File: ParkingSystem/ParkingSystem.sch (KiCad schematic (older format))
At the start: 73 parts, among them J1 PJ-002A, J2 0430450400, J3 Conn_ARM_JTAG_SWD_10, J4 Conn_01x04_Female, J5 0430450200, SW1 SW_Push, U1 R-78E5.0-1.0, U2 R-783.3-0.5, U3 STM32F103C4Tx, U5 74LS47, U6 74LS47, Y1 Crystal

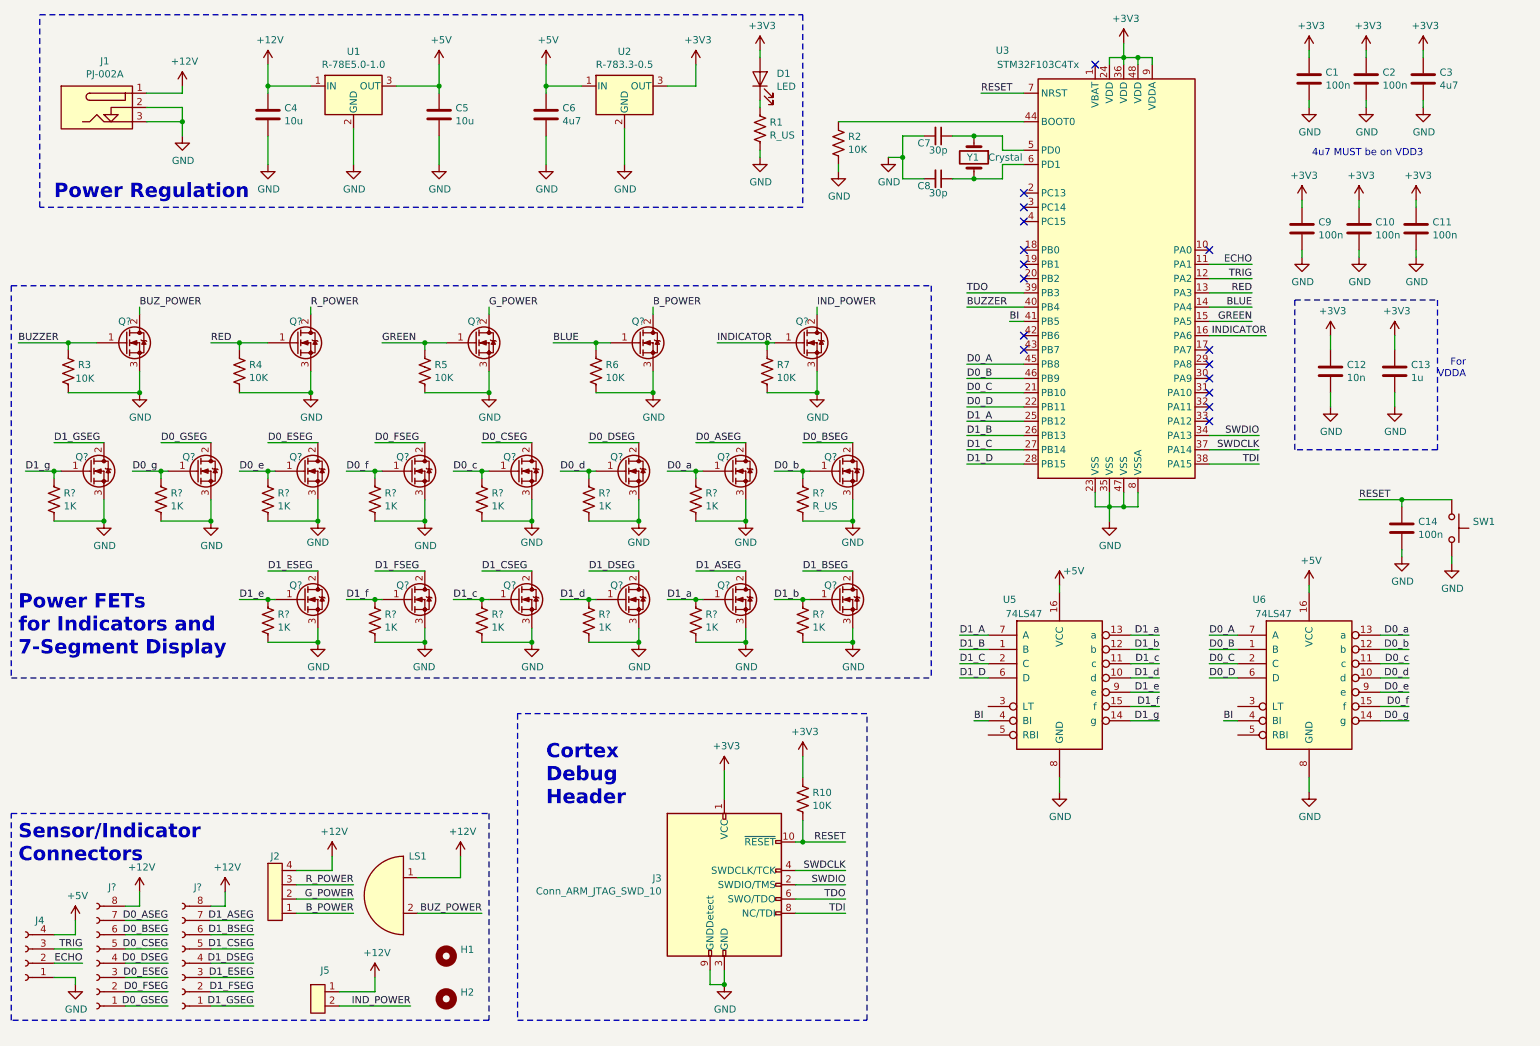
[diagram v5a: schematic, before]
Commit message: Create sn74L47 footprint and begin pcb layout
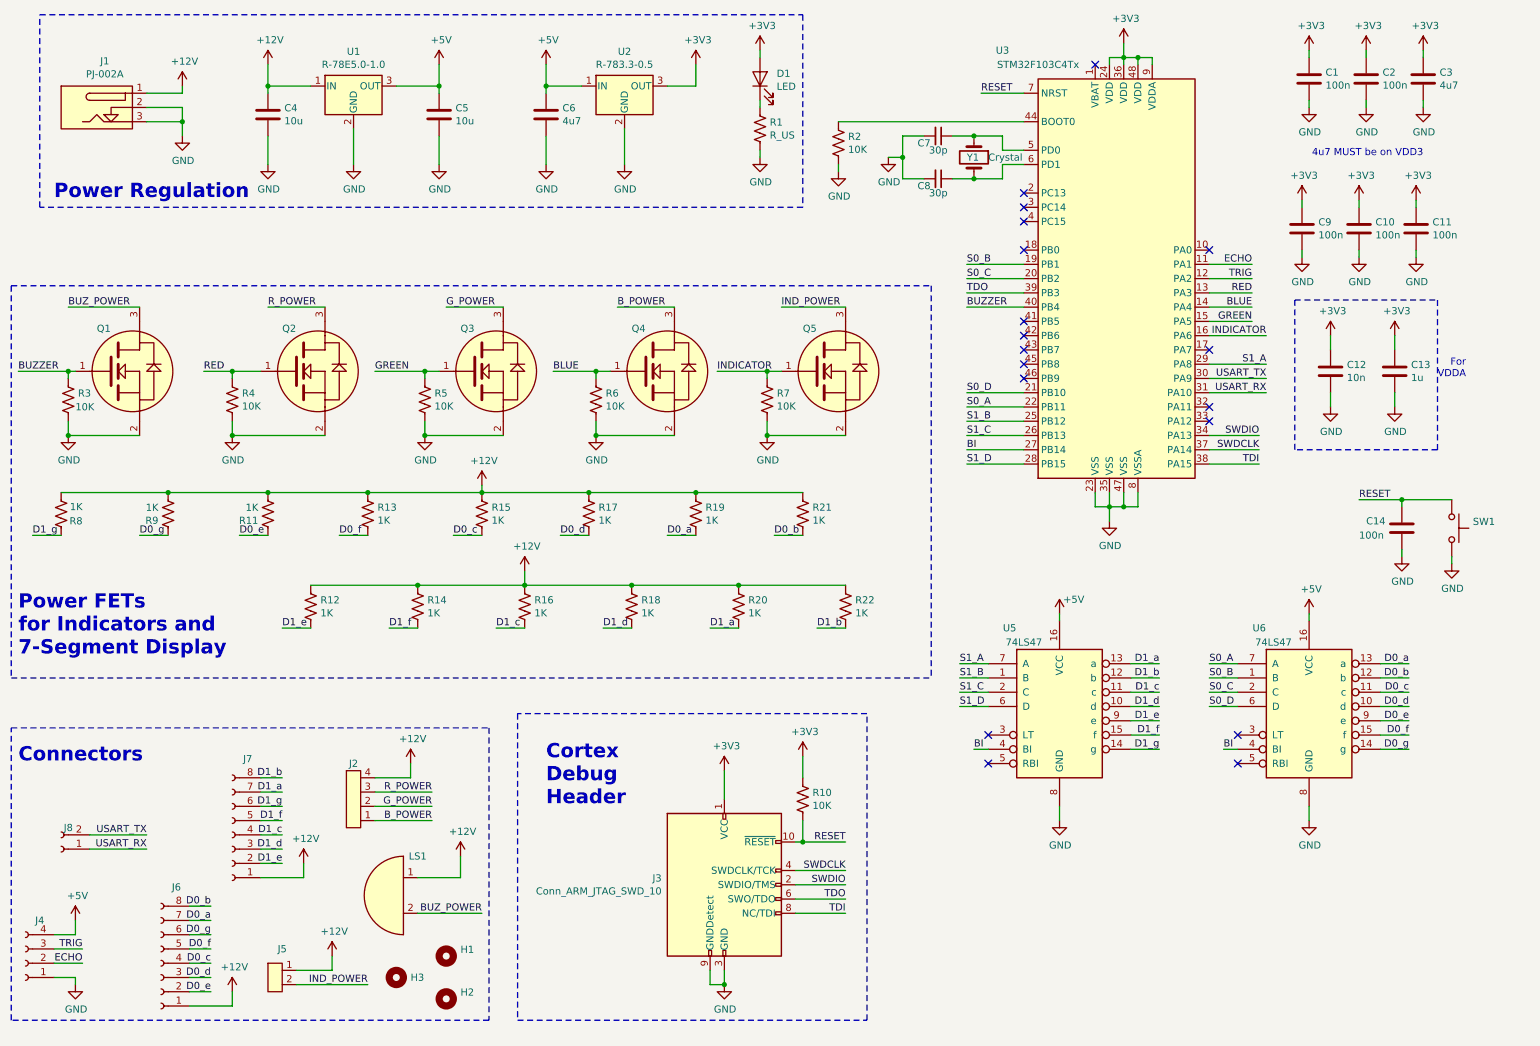
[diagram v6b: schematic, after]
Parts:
- removed Q? (x17): Q_NMOS_GDS, symbol Device:Q_NMOS_GDS
- removed Q? (x2): 1K, symbol Device:Q_NMOS_GDS
- added H3: MountingHole, MountingHole:MountingHole_4.3mm_M4_DIN965_Pad, symbol Mechanical:MountingHole
- added J8: Conn_01x02_Female, Connector_PinHeader_2.54mm:PinHeader_1x02_P2.54mm_Vertical, symbol Connector:Conn_01x02_Female
- added Q1, Q2, Q3, Q4, Q5: SSM3K333R,LF, MOSFETS:SSM3K33R,LF, symbol MOSFETS:SSM3K333R,LF
- J6, J7: renamed from J?; footprint (none) -> Connector_Molex:Molex_Micro-Fit_3.0_43045-0800_2x04_P3.00mm_Horizontal
- R11, R12, R13, R14, R15, R16, R17, R18, R19, R20, R22, R8, R9: renamed from R?; footprint (none) -> Resistor_SMD:R_0603_1608Metric_Pad1.05x0.95mm_HandSolder
- R21: renamed from R?; value R_US -> 1K; footprint (none) -> Resistor_SMD:R_0603_1608Metric_Pad1.05x0.95mm_HandSolder
- U5, U6: footprint (none) -> Drivers:SN74LS47N
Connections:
- net D0_ASEG is gone; now on net D0_a: J6.7 (Pin_7)
- net D0_BSEG is gone; now on net D0_g: J6.6 (Pin_6)
- net D0_CSEG is gone; now on net D0_f: J6.5 (Pin_5)
- net D0_DSEG is gone; now on net D0_c: J6.4 (Pin_4)
- net D0_ESEG is gone; now on net D0_d: J6.3 (Pin_3)
- net D0_FSEG is gone; now on net D0_e: J6.2 (Pin_2)
- net D0_GSEG is gone; now on net +12V: J6.1 (Pin_1)
- net D1_ASEG is gone; now on net D1_a: J7.7 (Pin_7)
- net D1_BSEG is gone; now on net D1_g: J7.6 (Pin_6)
- net D1_CSEG is gone; now on net D1_f: J7.5 (Pin_5)
- net D1_DSEG is gone; now on net D1_c: J7.4 (Pin_4)
- net D1_ESEG is gone; now on net D1_d: J7.3 (Pin_3)
- net D1_FSEG is gone; now on net D1_e: J7.2 (Pin_2)
- net D1_GSEG is gone; now on net +12V: J7.1 (Pin_1)
- net +12V: now also R11.2, R12.1, R13.1, R14.1, R15.1, R16.1, R17.1, R18.1, R19.1, R20.1, R21.1, R22.1, R8.2, R9.2; no longer J6.8 (Pin_8), J7.8 (Pin_8)
- net BI: now also U3.27 (PB14); no longer U3.41 (PB5)
- net BLUE: now also Q4.1
- net BUZZER: now also Q1.1
- net BUZ_POWER: now also Q1.3
- net B_POWER: now also Q4.3
- net D0_a: now also R19.2; no longer R19.1
- net D0_b: now also J6.8 (Pin_8), R21.2; no longer R21.1
- net D0_c: now also R15.2; no longer R15.1
- net D0_d: now also R17.2; no longer R17.1
- net D0_f: now also R13.2; no longer R13.1
- net D1_a: now also R20.2; no longer R20.1
- net D1_b: now also J7.8 (Pin_8), R22.2; no longer R22.1
- net D1_c: now also R16.2; no longer R16.1
- net D1_d: now also R18.2; no longer R18.1
- net D1_e: now also R12.2; no longer R12.1
- net D1_f: now also R14.2; no longer R14.1
- net GND: now also Q1.2, Q2.2, Q3.2, Q4.2, Q5.2; no longer R11.2, R12.2, R13.2, R14.2, R15.2, R16.2, R17.2, R18.2, R19.2, R20.2, R21.2, R22.2, R8.2, R9.2
- net GREEN: now also Q3.1
- net G_POWER: now also Q3.3
- net INDICATOR: now also Q5.1
- net IND_POWER: now also Q5.3
- net RED: now also Q2.1
- net R_POWER: now also Q2.3
- net S0_B: now reaches U3.19 (PB1)
- net S0_B: now also U6.1 (B)
- net S0_C: now reaches U3.20 (PB2)
- net S0_C: now also U6.2 (C)
- net S1_A: now reaches U3.29 (PA8)
- net S1_A: now also U5.7 (A)
- net USART_TX: now reaches U3.30 (PA9)
- net USART_TX: now also J8.2 (Pin_2)
- net USART_RX: now reaches U3.31 (PA10)
- net USART_RX: now also J8.1 (Pin_1)
- net D0_A: no longer names the net of U3.45 (PB8)
- net D0_A: no longer U6.7 (A)
- net D0_B: no longer names the net of U3.46 (PB9)
- net D0_B: no longer U6.1 (B)
- net D0_C renamed S0_D
- net S0_D: now also U6.6 (D); no longer U6.2 (C)
- net D0_D renamed S0_A
- net S0_A: now also U6.7 (A); no longer U6.6 (D)
- net D1_A renamed S1_B
- net S1_B: now also U5.1 (B); no longer U5.7 (A)
- net D1_B renamed S1_C
- net S1_C: now also U5.2 (C); no longer U5.1 (B)
- removed net D1_C: U3.27 (PB14), U5.2 (C)
- net D1_D renamed S1_D
- no-connect marks 16 -> 18
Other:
- note added: "Connectors"
- note removed: "Sensor/Indicator\nConnectors"
- moved on the sheet: J2, J5, J6, J7, R11, R12, R13, R14, R15, R16, R17, R18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

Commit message: Generate gerbers and BOM
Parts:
- Q1, Q2, Q3, Q4, Q5: symbol MOSFETS:SSM3K333R,LF -> ParkingSystem-rescue:SSM3K333R,LF-MOSFETS
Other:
- note added: "7-SEG Drivers"
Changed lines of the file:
@@
 EESchema Schematic File Version 4
 LIBS:ParkingSystem-cache
-EELAYER 26 0
+EELAYER 29 0
 EELAYER END
 $Descr A4 11693 8268
@@
 	3900 3950 3900 4000
 $Comp
-L MOSFETS:SSM3K333R,LF Q1
+L ParkingSystem-rescue:SSM3K333R,LF-MOSFETS Q1
 U 1 1 5CF42842
 P 1350 3150
@@
 Connection ~ 2150 3600
 $Comp
-L MOSFETS:SSM3K333R,LF Q2
+L ParkingSystem-rescue:SSM3K333R,LF-MOSFETS Q2
 U 1 1 5D0CEAA7
 P 2650 3150
@@
 Connection ~ 3500 3600
 $Comp
-L MOSFETS:SSM3K333R,LF Q3
+L ParkingSystem-rescue:SSM3K333R,LF-MOSFETS Q3
 U 1 1 5D16B49E
 P 3900 3150
@@
 Connection ~ 4700 3600
 $Comp
-L MOSFETS:SSM3K333R,LF Q4
+L ParkingSystem-rescue:SSM3K333R,LF-MOSFETS Q4
 U 1 1 5D23D1DB
 P 5100 3150
@@
 Connection ~ 5900 3600
 $Comp
-L MOSFETS:SSM3K333R,LF Q5
+L ParkingSystem-rescue:SSM3K333R,LF-MOSFETS Q5
 U 1 1 5D2B7F2A
 P 6300 3150
@@
 	1    0    0    -1
 $EndComp
+Wire Notes Line
+	7200 4600 10000 4600
+Wire Notes Line
+	10000 4600 10000 4900
+Wire Notes Line
+	10000 4900 10450 4900
+Wire Notes Line
+	10450 4900 10450 6500
+Wire Notes Line
+	10450 6500 7200 6500
+Wire Notes Line
+	7200 6500 7200 4600
+Text Notes 8300 4850 0    100  ~ 20
+7-SEG Drivers
 $EndSCHEMATC
